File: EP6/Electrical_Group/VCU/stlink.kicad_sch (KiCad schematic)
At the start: 32 parts, among them J16 STDC14, J2 Conn_01x06, J24 USB_C_stm32, J6 USB_SEL, SW2 VBUS, U1 USB3300-EZK, U14 LM66100DCK, U15 USBLC6-2SC6, Y3 X322524MSB4SI

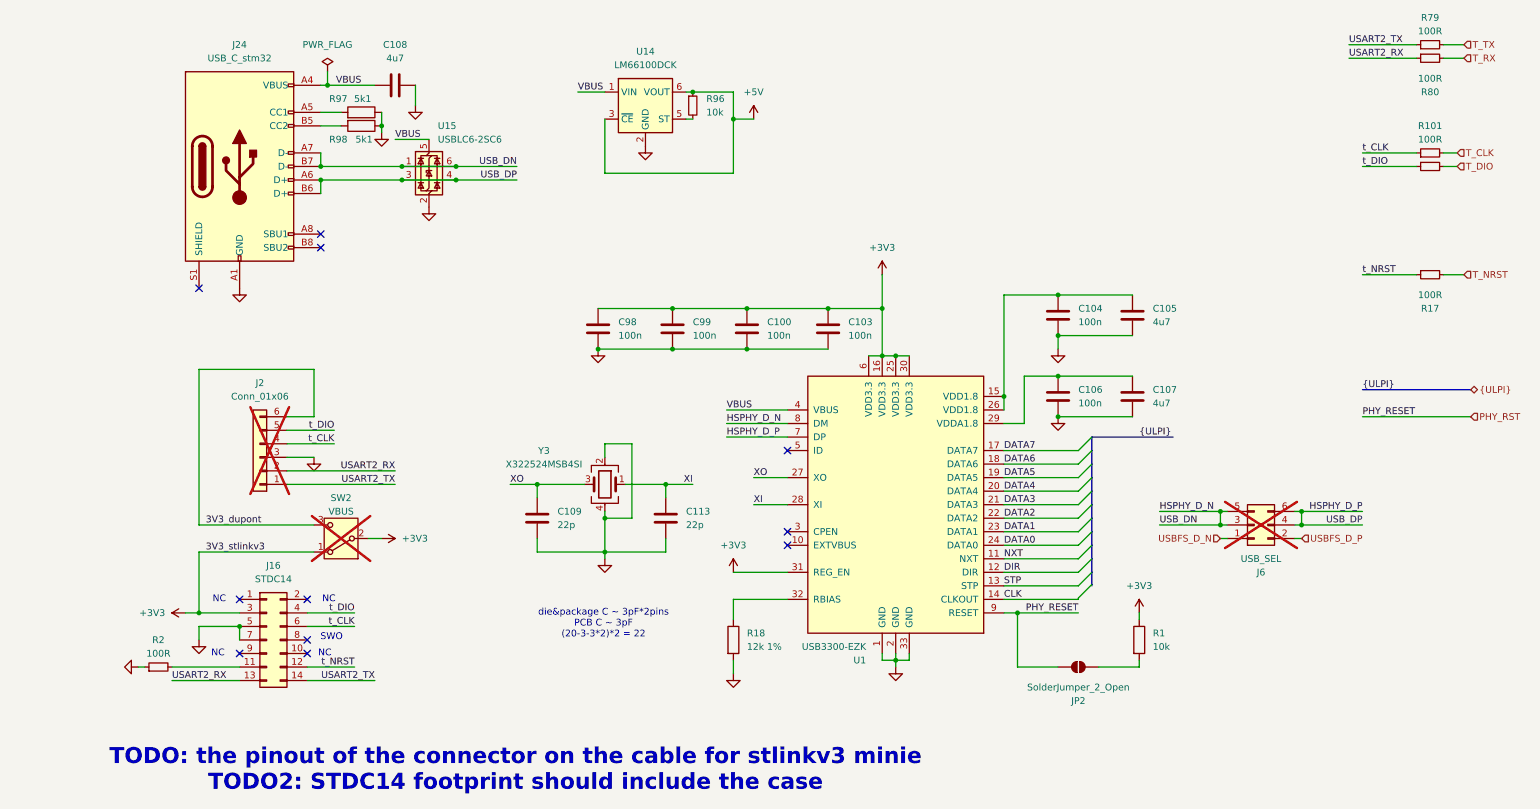
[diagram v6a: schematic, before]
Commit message: udpate VCU to V3.0
V3.0 move mounting point out a little
     remove HSUSB
     remove brake light
     change conn pinout to match dashboard V1.0
     add CAN2
     add some LEDs
     Etc.
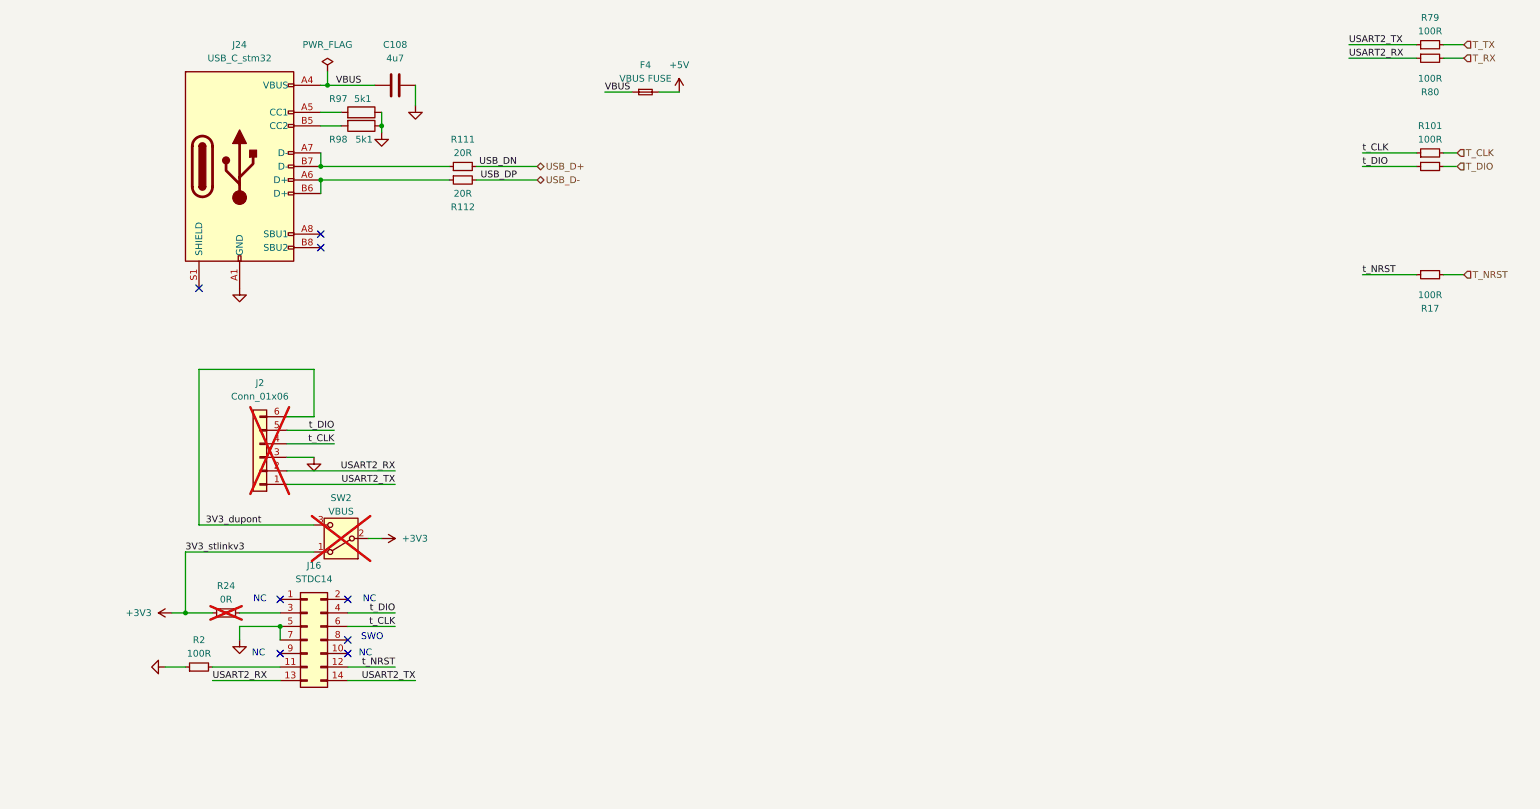
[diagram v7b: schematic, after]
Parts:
- removed C100, C103, C104, C106, C98, C99: 100n, Capacitor_SMD:C_0402_1005Metric, symbol Device:C
- removed C105, C107: 4u7, Capacitor_SMD:C_0402_1005Metric, symbol Device:C
- removed C109, C113: 22p, Capacitor_SMD:C_0402_1005Metric, symbol Device:C
- removed J6: USB_SEL, Connector_PinHeader_2.54mm:PinHeader_2x03_P2.54mm_Vertical_SMD, symbol Connector_Generic:Conn_02x03_Odd_Even
- removed JP2: SolderJumper_2_Open, Jumper:SolderJumper-2_P1.3mm_Open_RoundedPad1.0x1.5mm, symbol Jumper:SolderJumper_2_Open
- removed R1: 10k, Resistor_SMD:R_0402_1005Metric, symbol Device:R
- removed R18: 12k 1%, Resistor_SMD:R_0402_1005Metric, symbol Device:R
- removed R96: 10k, Resistor_SMD:R_0402_1005Metric, symbol Device:R_Small
- removed U1: USB3300-EZK, Package_DFN_QFN:QFN-32-1EP_5x5mm_P0.5mm_EP3.45x3.45mm, symbol Interface_USB:USB3300-EZK
- removed U14: LM66100DCK, Package_TO_SOT_SMD:SOT-363_SC-70-6, symbol Power_Management:LM66100DCK
- removed U15: USBLC6-2SC6, Package_TO_SOT_SMD:SOT-23-6, symbol Power_Protection:USBLC6-2SC6
- removed Y3: X322524MSB4SI, Crystal:Crystal_SMD_3225-4Pin_3.2x2.5mm, symbol Device:Crystal_GND24
- added F4: VBUS FUSE, Fuse:Fuse_1206_3216Metric, symbol Device:Fuse_Small
- added R111, R112: 20R, Resistor_SMD:R_0402_1005Metric, symbol Device:R_Small
- added R24: 0R, Resistor_SMD:R_0402_1005Metric, symbol Device:R_Small
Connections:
- net +3V3: now also R24.1; no longer J16.3 (Pin_3)
- net +5V: now also F4.2
- net VBUS: now also F4.1
- net HSPHY_D_N: no longer names the net of J24.A7 (D-), J24.B7 (D-)
- net HSPHY_D_N: now also R111.1
- net HSPHY_D_P: no longer names the net of J24.A6 (D+), J24.B6 (D+)
- net HSPHY_D_P: now also R112.1
- new net: J16.3 (Pin_3), R24.2
- new net USB_D+: R111.2
- new net USB_D-: R112.2
- no-connect marks 11 -> 8
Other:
- note removed: "TODO: the pinout of the connector on the cable for stlinkv3 minie TODO2: STDC14 footprint should include the case"
- note removed: "die&package C ~ 3pF*2pins PCB C ~ 3pF (20-3-3*2)*2 = 22"
- title: EP6 VCU -> VCU
- moved on the sheet: J16, R2

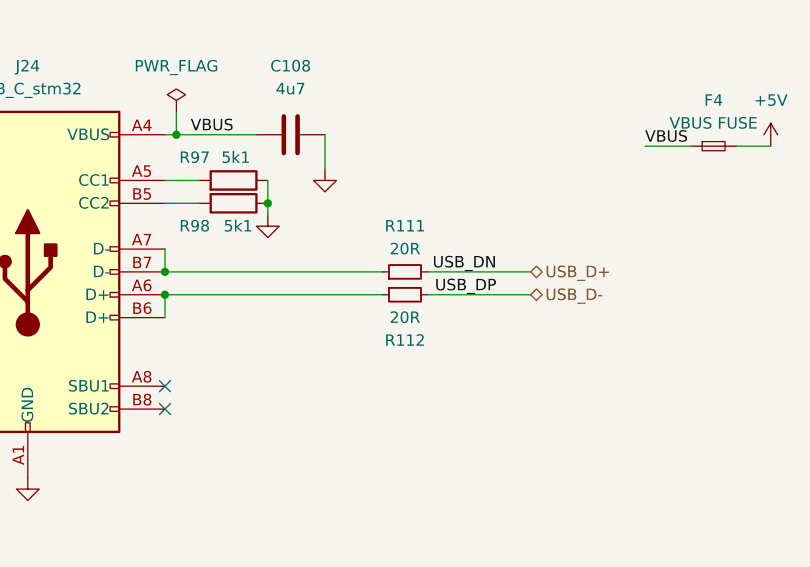
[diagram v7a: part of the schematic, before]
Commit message: update VCU
no version change
just update for some modification on schematic after JLCPCBA part selection
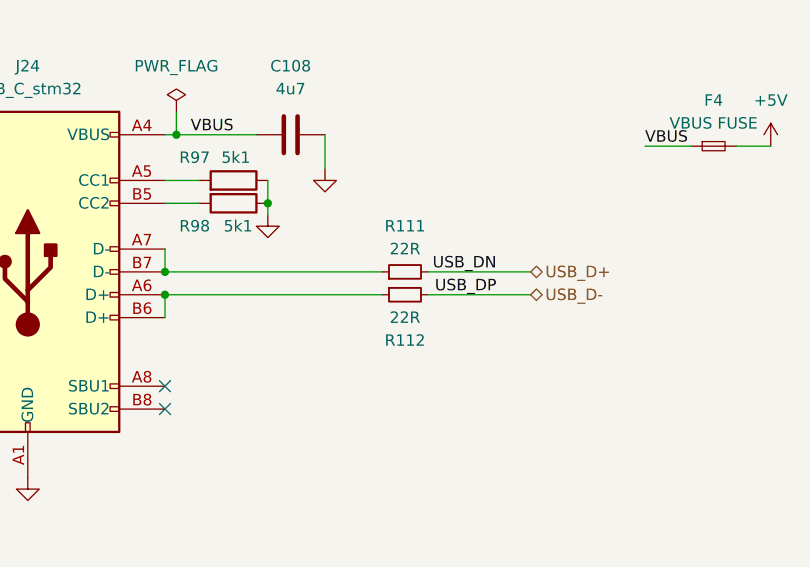
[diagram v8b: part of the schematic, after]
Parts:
- R111, R112: value 20R -> 22R
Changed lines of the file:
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@@
 			)
 		)
-		(property "Value" "20R"
+		(property "Value" "22R"
 			(at 76.2 53.34 90)
 			(effects
@@
 			)
 		)
-		(property "Value" "20R"
+		(property "Value" "22R"
 			(at 76.2 45.72 90)
 			(effects
